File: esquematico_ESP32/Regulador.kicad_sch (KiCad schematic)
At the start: 8 parts, among them U3 LM2596S-5

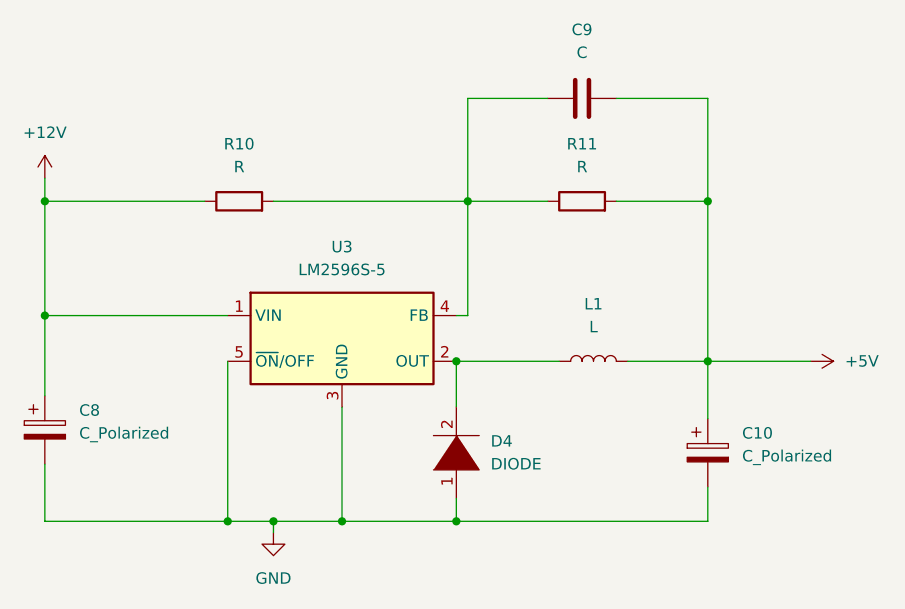
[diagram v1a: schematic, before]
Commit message: se agregaron los valores (pendiente última revisión)
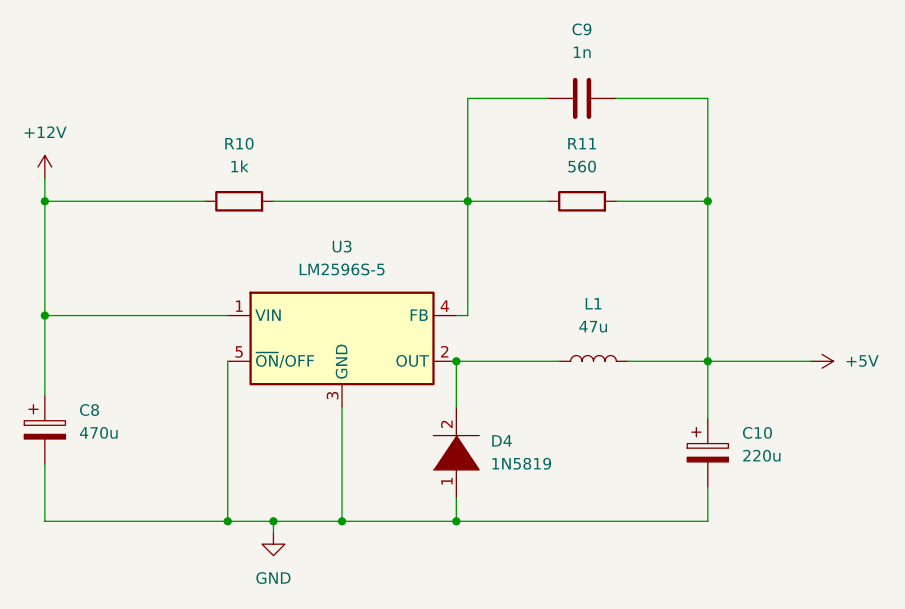
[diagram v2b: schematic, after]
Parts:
- C10: value C_Polarized -> 220u
- C8: value C_Polarized -> 470u
- C9: value C -> 1n
- D4: value DIODE -> 1N5819
- L1: value L -> 47u
- R10: value R -> 1k
- R11: value R -> 560
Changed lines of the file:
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@@
     (in_bom yes) (on_board yes) (fields_autoplaced)
     (property "Reference" "L1" (id 0) (at 166.37 77.47 90))
-    (property "Value" "L" (id 1) (at 166.37 80.01 90))
+    (property "Value" "47u" (id 1) (at 166.37 80.01 90))
     (property "Footprint" "Inductor_SMD:L_Neosid_SM-PIC0612H" (id 2) (at 166.37 83.82 0)
       (effects (font (size 1.27 1.27)) hide)
@@
     (in_bom yes) (on_board yes) (fields_autoplaced)
     (property "Reference" "R10" (id 0) (at 127 59.69 90))
-    (property "Value" "R" (id 1) (at 127 62.23 90))
+    (property "Value" "1k" (id 1) (at 127 62.23 90))
     (property "Footprint" "Resistor_SMD:R_0805_2012Metric_Pad1.20x1.40mm_HandSolder" (id 2) (at 127 67.818 90)
       (effects (font (size 1.27 1.27)) hide)
@@
       (effects (font (size 1.27 1.27)) (justify left))
     )
-    (property "Value" "C_Polarized" (id 1) (at 182.88 94.3609 0)
+    (property "Value" "220u" (id 1) (at 182.88 94.3609 0)
       (effects (font (size 1.27 1.27)) (justify left))
     )
@@
     (in_bom yes) (on_board yes) (fields_autoplaced)
     (property "Reference" "R11" (id 0) (at 165.1 59.69 90))
-    (property "Value" "R" (id 1) (at 165.1 62.23 90))
+    (property "Value" "560" (id 1) (at 165.1 62.23 90))
     (property "Footprint" "Resistor_SMD:R_0805_2012Metric_Pad1.20x1.40mm_HandSolder" (id 2) (at 165.1 67.818 90)
       (effects (font (size 1.27 1.27)) hide)
@@
       (effects (font (size 1.27 1.27)) (justify right))
     )
-    (property "Value" "DIODE" (id 1) (at 154.94 95.2499 90)
+    (property "Value" "1N5819" (id 1) (at 154.94 95.2499 90)
       (effects (font (size 1.27 1.27)) (justify right))
     )
@@
     (in_bom yes) (on_board yes) (fields_autoplaced)
     (property "Reference" "C9" (id 0) (at 165.1 46.99 90))
-    (property "Value" "C" (id 1) (at 165.1 49.53 90))
+    (property "Value" "1n" (id 1) (at 165.1 49.53 90))
     (property "Footprint" "Capacitor_SMD:C_0805_2012Metric_Pad1.18x1.45mm_HandSolder" (id 2) (at 168.91 53.6448 0)
       (effects (font (size 1.27 1.27)) hide)
@@
       (effects (font (size 1.27 1.27)) (justify left))
     )
-    (property "Value" "C_Polarized" (id 1) (at 109.22 91.8209 0)
+    (property "Value" "470u" (id 1) (at 109.22 91.8209 0)
       (effects (font (size 1.27 1.27)) (justify left))
     )

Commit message: .
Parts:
- removed C9: 1n, Capacitor_SMD:C_0805_2012Metric_Pad1.18x1.45mm_HandSolder, symbol Device:C
- removed R10: 1k, Resistor_SMD:R_0805_2012Metric_Pad1.20x1.40mm_HandSolder, symbol Device:R
- removed R11: 560, Resistor_SMD:R_0805_2012Metric_Pad1.20x1.40mm_HandSolder, symbol Device:R
- D4: value 1N5819 -> 1N5825
- L1: value 47u -> 68u
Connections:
- net +5V: now also U3.4 (FB)
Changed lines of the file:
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@@
 (kicad_sch (version 20211123) (generator eeschema)
   (paper "A4")
-  (junction (at 105.41 66.04) (diameter 0) (color 0 0 0 0)
-  )
   (junction (at 105.41 78.74) (diameter 0) (color 0 0 0 0)
   )
@@
   (junction (at 125.73 101.6) (diameter 0) (color 0 0 0 0)
   )
-  (junction (at 179.07 66.04) (diameter 0) (color 0 0 0 0)
-  )
   (junction (at 151.13 83.82) (diameter 0) (color 0 0 0 0)
   )
   (junction (at 130.81 101.6) (diameter 0) (color 0 0 0 0)
   )
-  (junction (at 152.4 66.04) (diameter 0) (color 0 0 0 0)
-  )
-  (wire (pts (xy 161.29 54.61) (xy 152.4 54.61))
-    (stroke (width 0) (type default) (color 0 0 0 0))
-  )
-  (wire (pts (xy 179.07 54.61) (xy 179.07 66.04))
-    (stroke (width 0) (type default) (color 0 0 0 0))
-  )
   (wire (pts (xy 130.81 101.6) (xy 138.43 101.6))
     (stroke (width 0) (type default) (color 0 0 0 0))
   )
-  (wire (pts (xy 152.4 66.04) (xy 161.29 66.04))
+  (wire (pts (xy 179.07 83.82) (xy 179.07 78.74))
     (stroke (width 0) (type default) (color 0 0 0 0))
   )
@@
     (stroke (width 0) (type default) (color 0 0 0 0))
   )
-  (wire (pts (xy 168.91 54.61) (xy 179.07 54.61))
+  (wire (pts (xy 151.13 78.74) (xy 179.07 78.74))
     (stroke (width 0) (type default) (color 0 0 0 0))
   )
   (wire (pts (xy 179.07 101.6) (xy 179.07 97.79))
-    (stroke (width 0) (type default) (color 0 0 0 0))
-  )
-  (wire (pts (xy 151.13 78.74) (xy 152.4 78.74))
     (stroke (width 0) (type default) (color 0 0 0 0))
   )
@@
     (stroke (width 0) (type default) (color 0 0 0 0))
   )
-  (wire (pts (xy 168.91 66.04) (xy 179.07 66.04))
-    (stroke (width 0) (type default) (color 0 0 0 0))
-  )
   (wire (pts (xy 179.07 83.82) (xy 179.07 90.17))
     (stroke (width 0) (type default) (color 0 0 0 0))
   )
-  (wire (pts (xy 105.41 66.04) (xy 105.41 78.74))
+  (wire (pts (xy 105.41 63.5) (xy 105.41 78.74))
     (stroke (width 0) (type default) (color 0 0 0 0))
   )
@@
     (stroke (width 0) (type default) (color 0 0 0 0))
   )
-  (wire (pts (xy 152.4 66.04) (xy 152.4 78.74))
-    (stroke (width 0) (type default) (color 0 0 0 0))
-  )
   (wire (pts (xy 170.18 83.82) (xy 179.07 83.82))
-    (stroke (width 0) (type default) (color 0 0 0 0))
-  )
-  (wire (pts (xy 130.81 66.04) (xy 152.4 66.04))
     (stroke (width 0) (type default) (color 0 0 0 0))
   )
@@
     (stroke (width 0) (type default) (color 0 0 0 0))
   )
-  (wire (pts (xy 105.41 63.5) (xy 105.41 66.04))
-    (stroke (width 0) (type default) (color 0 0 0 0))
-  )
   (wire (pts (xy 179.07 83.82) (xy 190.5 83.82))
-    (stroke (width 0) (type default) (color 0 0 0 0))
-  )
-  (wire (pts (xy 179.07 66.04) (xy 179.07 83.82))
-    (stroke (width 0) (type default) (color 0 0 0 0))
-  )
-  (wire (pts (xy 123.19 66.04) (xy 105.41 66.04))
     (stroke (width 0) (type default) (color 0 0 0 0))
   )
@@
     (stroke (width 0) (type default) (color 0 0 0 0))
   )
-  (wire (pts (xy 152.4 54.61) (xy 152.4 66.04))
-    (stroke (width 0) (type default) (color 0 0 0 0))
-  )
   (symbol (lib_id "Device:L") (at 166.37 83.82 90) (unit 1)
     (in_bom yes) (on_board yes) (fields_autoplaced)
     (property "Reference" "L1" (id 0) (at 166.37 77.47 90))
-    (property "Value" "47u" (id 1) (at 166.37 80.01 90))
+    (property "Value" "68u" (id 1) (at 166.37 80.01 90))
     (property "Footprint" "Inductor_SMD:L_Neosid_SM-PIC0612H" (id 2) (at 166.37 83.82 0)
       (effects (font (size 1.27 1.27)) hide)
     )
     (property "Datasheet" "~" (id 3) (at 166.37 83.82 0)
-      (effects (font (size 1.27 1.27)) hide)
-    )
-    (pin "1")
-    (pin "2")
-  )
-  (symbol (lib_id "Device:R") (at 127 66.04 90) (unit 1)
-    (in_bom yes) (on_board yes) (fields_autoplaced)
-    (property "Reference" "R10" (id 0) (at 127 59.69 90))
-    (property "Value" "1k" (id 1) (at 127 62.23 90))
-    (property "Footprint" "Resistor_SMD:R_0805_2012Metric_Pad1.20x1.40mm_HandSolder" (id 2) (at 127 67.818 90)
-      (effects (font (size 1.27 1.27)) hide)
-    )
-    (property "Datasheet" "~" (id 3) (at 127 66.04 0)
       (effects (font (size 1.27 1.27)) hide)
     )
@@
     (pin "2")
   )
-  (symbol (lib_id "Device:R") (at 165.1 66.04 90) (unit 1)
-    (in_bom yes) (on_board yes) (fields_autoplaced)
-    (property "Reference" "R11" (id 0) (at 165.1 59.69 90))
-    (property "Value" "560" (id 1) (at 165.1 62.23 90))
-    (property "Footprint" "Resistor_SMD:R_0805_2012Metric_Pad1.20x1.40mm_HandSolder" (id 2) (at 165.1 67.818 90)
-      (effects (font (size 1.27 1.27)) hide)
-    )
-    (property "Datasheet" "~" (id 3) (at 165.1 66.04 0)
-      (effects (font (size 1.27 1.27)) hide)
-    )
-    (pin "1")
-    (pin "2")
-  )
   (symbol (lib_id "pspice:DIODE") (at 151.13 93.98 90) (unit 1)
     (in_bom yes) (on_board yes) (fields_autoplaced)
@@
       (effects (font (size 1.27 1.27)) (justify right))
     )
-    (property "Value" "1N5819" (id 1) (at 154.94 95.2499 90)
+    (property "Value" "1N5825" (id 1) (at 154.94 95.2499 90)
       (effects (font (size 1.27 1.27)) (justify right))
     )
@@
       (effects (font (size 1.27 1.27)) hide)
     )
-    (pin "1")
-    (pin "2")
-  )
-  (symbol (lib_id "Device:C") (at 165.1 54.61 90) (unit 1)
-    (in_bom yes) (on_board yes) (fields_autoplaced)
-    (property "Reference" "C9" (id 0) (at 165.1 46.99 90))
-    (property "Value" "1n" (id 1) (at 165.1 49.53 90))
-    (property "Footprint" "Capacitor_SMD:C_0805_2012Metric_Pad1.18x1.45mm_HandSolder" (id 2) (at 168.91 53.6448 0)
-      (effects (font (size 1.27 1.27)) hide)
-    )
-    (property "Datasheet" "~" (id 3) (at 165.1 54.61 0)
-      (effects (font (size 1.27 1.27)) hide)
-    )

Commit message: Correciones de la clase
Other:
- moved on the sheet: C10
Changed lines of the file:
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@@
     (stroke (width 0) (type default) (color 0 0 0 0))
   )
-  (wire (pts (xy 179.07 101.6) (xy 179.07 97.79))
+  (wire (pts (xy 179.07 101.6) (xy 179.07 95.885))
     (stroke (width 0) (type default) (color 0 0 0 0))
   )
@@
     (stroke (width 0) (type default) (color 0 0 0 0))
   )
-  (wire (pts (xy 179.07 83.82) (xy 179.07 90.17))
+  (wire (pts (xy 179.07 83.82) (xy 179.07 88.265))
     (stroke (width 0) (type default) (color 0 0 0 0))
   )
@@
     (pin "1")
   )
-  (symbol (lib_id "Device:C_Polarized") (at 179.07 93.98 0) (unit 1)
+  (symbol (lib_id "Device:C_Polarized") (at 179.07 92.075 0) (unit 1)
     (in_bom yes) (on_board yes) (fields_autoplaced)
-    (property "Reference" "C10" (id 0) (at 182.88 91.8209 0)
+    (property "Reference" "C10" (id 0) (at 182.88 89.9159 0)
       (effects (font (size 1.27 1.27)) (justify left))
     )
-    (property "Value" "220u" (id 1) (at 182.88 94.3609 0)
+    (property "Value" "220u" (id 1) (at 182.88 92.4559 0)
       (effects (font (size 1.27 1.27)) (justify left))
     )
-    (property "Footprint" "Capacitor_SMD:CP_Elec_8x6.9" (id 2) (at 180.0352 97.79 0)
+    (property "Footprint" "Capacitor_SMD:CP_Elec_8x6.9" (id 2) (at 180.0352 95.885 0)
       (effects (font (size 1.27 1.27)) hide)
     )
-    (property "Datasheet" "~" (id 3) (at 179.07 93.98 0)
+    (property "Datasheet" "~" (id 3) (at 179.07 92.075 0)
       (effects (font (size 1.27 1.27)) hide)
     )

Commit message: Alternativa_Acomodada
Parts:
- C10: footprint Capacitor_SMD:CP_Elec_8x6.9 -> Capacitor_SMD:CP_Elec_6.3x7.7
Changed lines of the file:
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@@
       (effects (font (size 1.27 1.27)) (justify left))
     )
-    (property "Footprint" "Capacitor_SMD:CP_Elec_8x6.9" (id 2) (at 180.0352 95.885 0)
+    (property "Footprint" "Capacitor_SMD:CP_Elec_6.3x7.7" (id 2) (at 180.0352 95.885 0)
       (effects (font (size 1.27 1.27)) hide)
     )

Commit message: placa terminada
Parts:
- D4: footprint Diode_THT:D_DO-27_P12.70mm_Horizontal -> Diode_THT:D_DO-201AE_P5.08mm_Vertical_AnodeUp
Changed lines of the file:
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@@
       (effects (font (size 1.27 1.27)) (justify right))
     )
-    (property "Footprint" "Diode_THT:D_DO-27_P12.70mm_Horizontal" (id 2) (at 151.13 93.98 0)
+    (property "Footprint" "Diode_THT:D_DO-201AE_P5.08mm_Vertical_AnodeUp" (id 2) (at 151.13 93.98 0)
       (effects (font (size 1.27 1.27)) hide)
     )
